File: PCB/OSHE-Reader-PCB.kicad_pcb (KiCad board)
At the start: 4 copper layers, 115 x 100 mm, 96 parts, among them J1 2171750001, J2 112L-TDA0, J3 Conn_01x24_MountingPin, J4 S2B-PH-K-SLFSN, Q1 Q_PNP_BCEC, Q2 Si1308EDL, SW1 SW_Push, SW2 SW_Push, SW3 SW_Push, SW4 SW_Push, SW5 SW_Push, U1 BQ2057CSNTR, U2 IRF7326D2TRPBF, U3 TPS5432DDAR

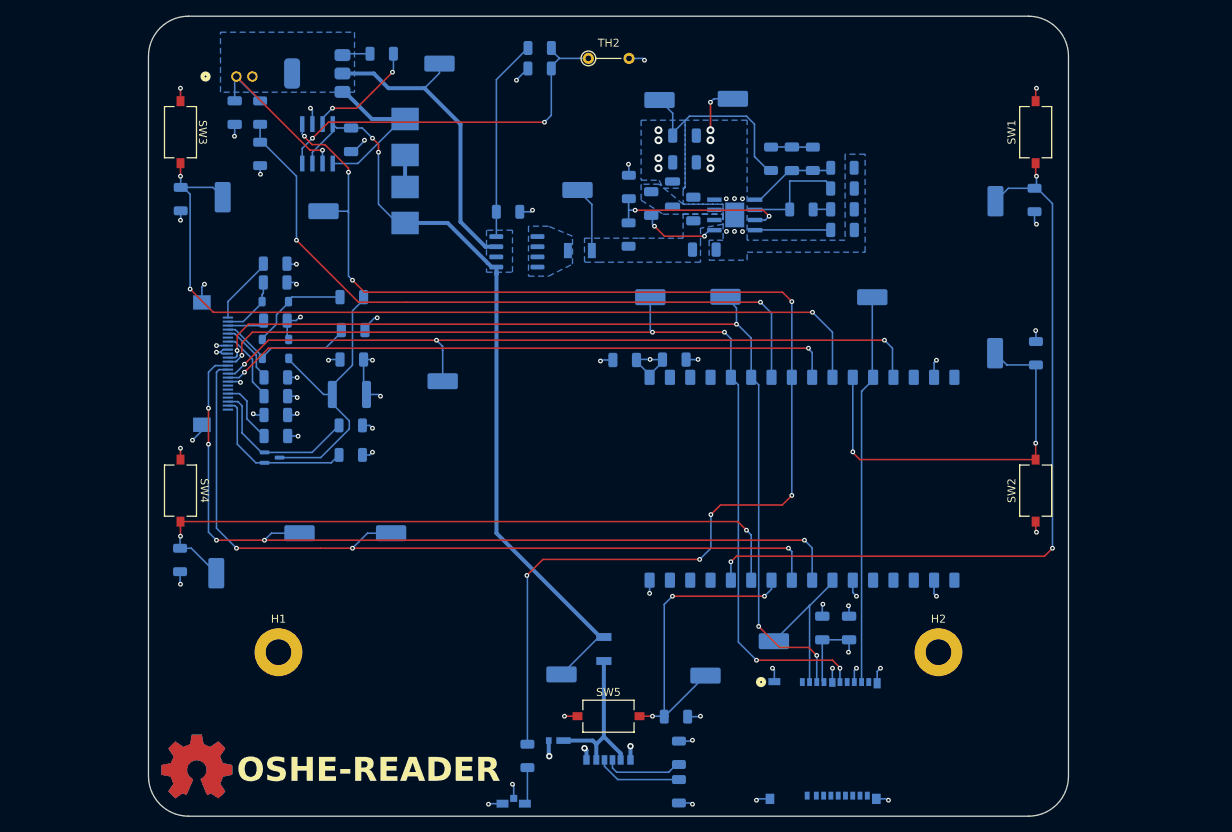
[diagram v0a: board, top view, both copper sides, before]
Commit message: Shuffled display connector around for fitting EPD ribbon cable position (also imported dxf for screen + bracket)
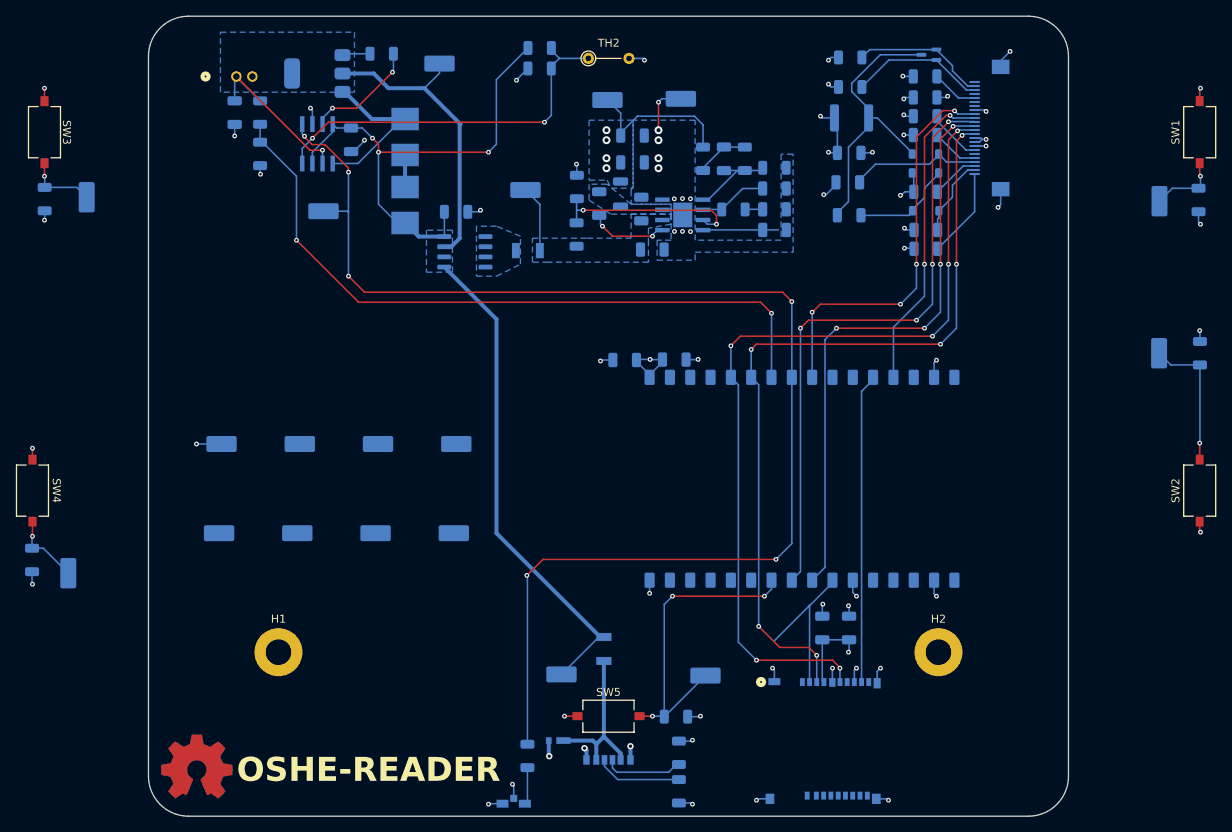
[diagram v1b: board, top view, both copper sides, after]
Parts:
- added TP_GND2: TestPoint, TestPoint:TestPoint_Keystone_5019_Miniature, B.Cu at (41.6, 134.0)
- R19: value 0.47R -> 0.47
- R20, TH2: value 10K -> 10k
- R21, R22: value 1M -> 100k
- R6: value 100K -> 100k
- moved J3 104.4 mm to (139.2, 94.5), turned to 90 degrees
- moved Q2 96.3 mm to (130.1, 85.3), turned to 180 degrees
- moved C17 92.8 mm to (129.6, 88.0), turned to 180 degrees
- moved C18 90.3 mm to (129.6, 90.7), turned to 180 degrees
- moved C19 88.4 mm to (129.6, 93.0), turned to 180 degrees
- moved C20 86.6 mm to (129.6, 95.4), turned to 180 degrees
- moved D2 85.2 mm to (129.6, 97.7), turned to 180 degrees
- moved D3 83.9 mm to (129.6, 100.1), turned to 0 degrees
- moved C21 82.9 mm to (129.6, 102.5), turned to 180 degrees
- moved D1 82.1 mm to (129.6, 104.8), turned to 0 degrees
- moved C22 81.6 mm to (129.7, 107.2), turned to 180 degrees
- moved C23 81.4 mm to (129.7, 109.6), turned to 180 degrees
- moved R20 79.8 mm to (120.2, 85.7), turned to 180 degrees
- moved R19 75.4 mm to (120.2, 89.3), turned to 180 degrees
- moved L2 71.7 mm to (120.4, 93.2), turned to 0 degrees
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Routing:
- net /Buttons/UpButton: track 110.3 -> 8.79 mm, vias 3 -> 1
- net /Buttons/LeftButton: track 98.1 -> 8.83 mm, vias 3 -> 1
- net /Buttons/DownButton: track 86.9 -> 9.17 mm, vias 2 -> 1
- net /EP_RESET: track 94.4 -> 39.2 mm, vias 3 -> 2
- net /EP_CS: track 107.8 -> 73.2 mm, vias 5 -> 4
- net /Buttons/RightButton: track 50.2 -> 17.6 mm, vias 2 -> 1
- net /EP_BUSY: track 77.9 -> 50.1 mm, vias 2 -> 4
- net /EP_D/C: track 103.4 -> 76.6 mm, vias 3 -> 4
- net /COPI: track 122.0 -> 99.9 mm, vias 4 -> 6
- net /SCK: track 124.5 -> 108.1 mm, vias 5 -> 6
- net /CIPO: track 48.7 -> 38.8 mm
- net Net-(U3-COMP): track 13.6 -> 8.55 mm
- net +3V3: track 62.8 -> 58.9 mm
- net /Display Connector/GDR: track 19.9 -> 16.8 mm
- net GND: track 91.7 -> 94.7 mm, vias 60 -> 61
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
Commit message: Did a bunch of work: - Updated footprint libs with proper 3d models to fix models dissapearing on update from pcb - Updated footprint libs with better silkscreen for drc - Re-did ESP32-C6 Footprint to support through hole AND castellated edges (espressif & waveshare) - Rerouted PCB around new MCU footprint - Minor cleanup on schematic + extra GND test point for convienience using O-Scope
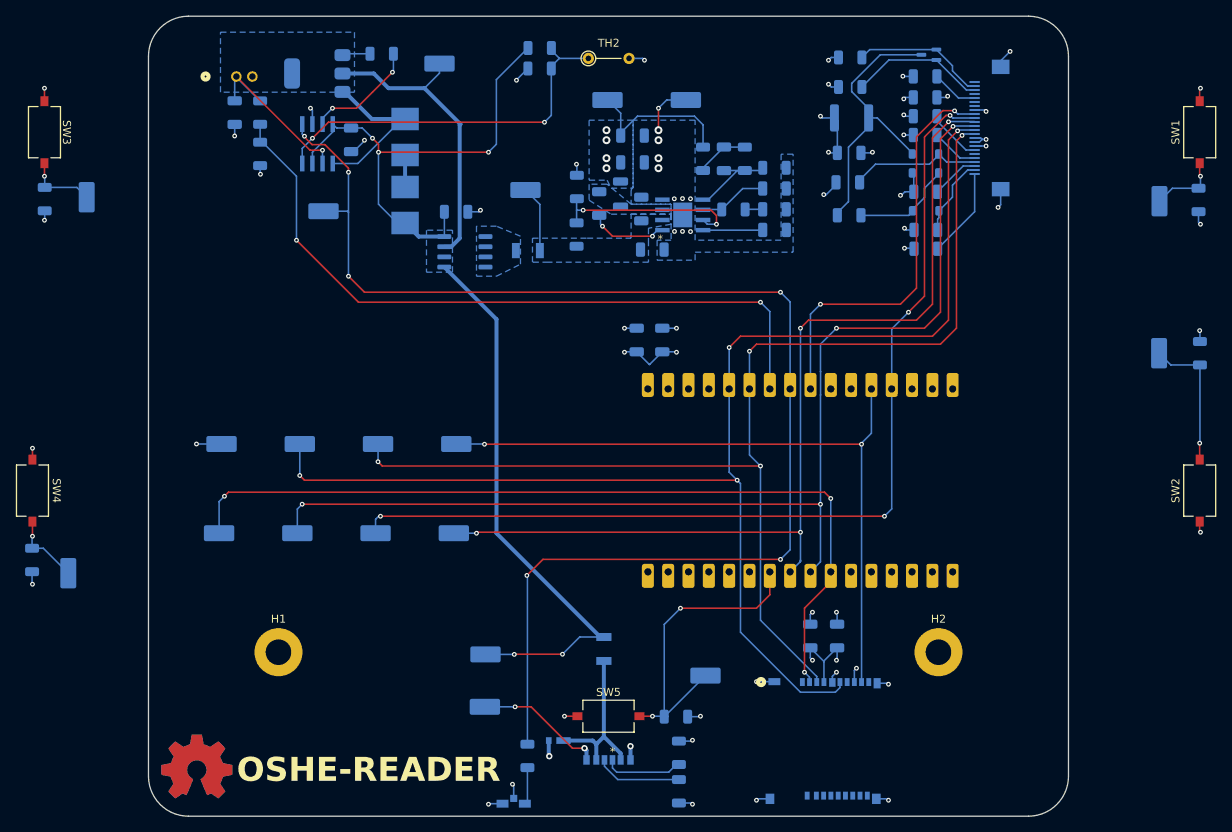
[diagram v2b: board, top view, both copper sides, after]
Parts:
- added TP_GND2: TestPoint, TestPoint:TestPoint_Keystone_5019_Miniature, B.Cu at (99.7, 91.0)
- moved TP_GND1 79.9 mm to (74.5, 166.8)
- moved TP_VBUS1 9.82 mm to (74.6, 160.3)
- moved C12 2.92 mm to (93.5, 121.0), turned to 90 degrees
- moved C13 2.87 mm to (96.7, 121.0), turned to 90 degrees
- moved C24 1.80 mm to (118.6, 158.0)
- moved C25 1.80 mm to (115.2, 158.0)
- moved U4 0.30 mm to (117.5, 138.5)
- renumbered TP_GND2 to TP_GND3
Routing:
- net /SD_CS: track 20.3 -> 108.6 mm, vias 0 -> 3
- net /EP_RESET: track 39.2 -> 122.5 mm, vias 2 -> 4
- net /EP_CS: track 73.2 -> 140.9 mm
- net /SCK: track 108.1 -> 166.6 mm, vias 6 -> 4
- net /CIPO: track 38.8 -> 88.3 mm, vias 0 -> 2
- net /COPI: track 99.9 -> 148.2 mm, vias 6 -> 4
- net /EP_D/C: track 76.6 -> 119.2 mm
- net /Battery Charging/VBUS: track 124.6 -> 133.1 mm, vias 3 -> 5
- net GND: track 94.7 -> 101.3 mm, vias 61 -> 58
- net Net-(U3-SS): track 9.46 -> 7.50 mm
- net /EP_BUSY: track 50.1 -> 51.7 mm, vias 4 -> 2
- net Net-(U4-GPIO0): track 87.7 -> 89.1 mm
- net +3V3: track 58.9 -> 58.1 mm, vias 15 -> 17
- net /Buttons/HomeButton: track 40.2 -> 40.0 mm, vias 3 -> 2

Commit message: Last updates for PCB order. Added revision number, fanicied logo, finished button positions, TODO: Blizzard T. Husky signature :P
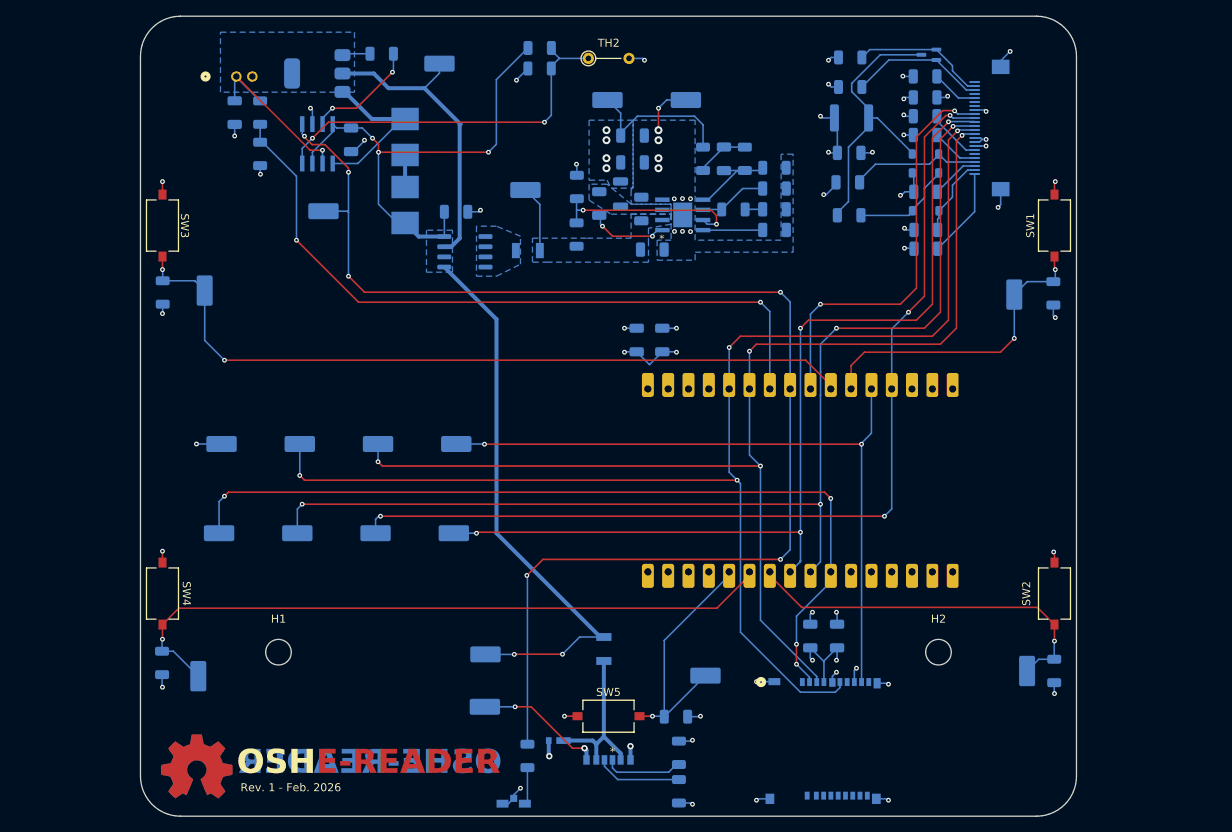
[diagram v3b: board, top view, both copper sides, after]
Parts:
- moved R17 43.7 mm to (145.7, 162.3), turned to -90 degrees
- moved TP_RIGHT1 43.0 mm to (142.3, 162.3)
- moved SW2 22.3 mm to (145.8, 152.7), turned to -90 degrees
- moved R16 21.6 mm to (145.6, 115.1)
- moved SW1 21.6 mm to (145.8, 106.7)
- moved TP_LEFT1 21.6 mm to (140.7, 115.3)
- moved R15 20.7 mm to (34.2, 161.3)
- moved SW4 20.7 mm to (34.2, 152.7)
- moved TP_DOWN1 20.7 mm to (38.7, 163.0)
- moved SW3 18.8 mm to (34.2, 106.7)
- moved TP_UP1 18.8 mm to (39.5, 114.8)
- moved R14 18.8 mm to (34.3, 115.0)
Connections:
- U4 pad 11: /Buttons/RightButton -> /Buttons/LeftButton
- U4 pad 21: /Buttons/LeftButton -> /Buttons/HomeButton
- U4 pad 23: /Buttons/HomeButton -> /Buttons/RightButton
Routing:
- net /Buttons/UpButton: track 8.79 -> 96.1 mm, vias 1 -> 2
- net /Buttons/DownButton: track 9.17 -> 85.5 mm
- net /Buttons/LeftButton: track 8.83 -> 39.0 mm, vias 1 -> 2
- net /Buttons/RightButton: track 17.6 -> 46.9 mm
- net /Buttons/HomeButton: track 40.0 -> 32.4 mm, vias 2 -> 1
- net /SD_CS: track 108.6 -> 109.4 mm, vias 3 -> 4
- net GND: track 101.3 -> 100.9 mm, vias 58 -> 57
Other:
- board size 115 x 100 mm -> 117 x 100 mm
- board text added: "E-READER"
- board text added: "OSH"
- board text added: "Rev. 1 - Feb. 2026"

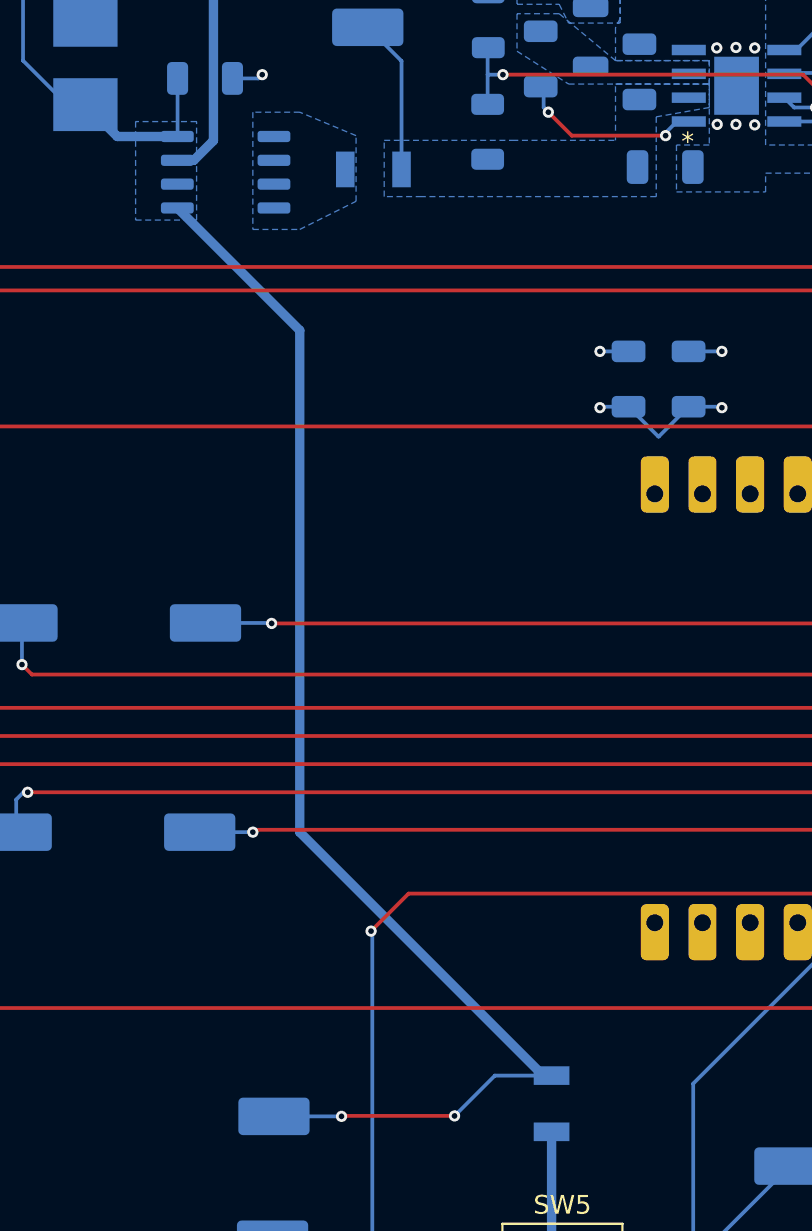
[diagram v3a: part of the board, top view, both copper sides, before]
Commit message: PCB and Schematic update
added the Schottky diode to PCB and Schematic
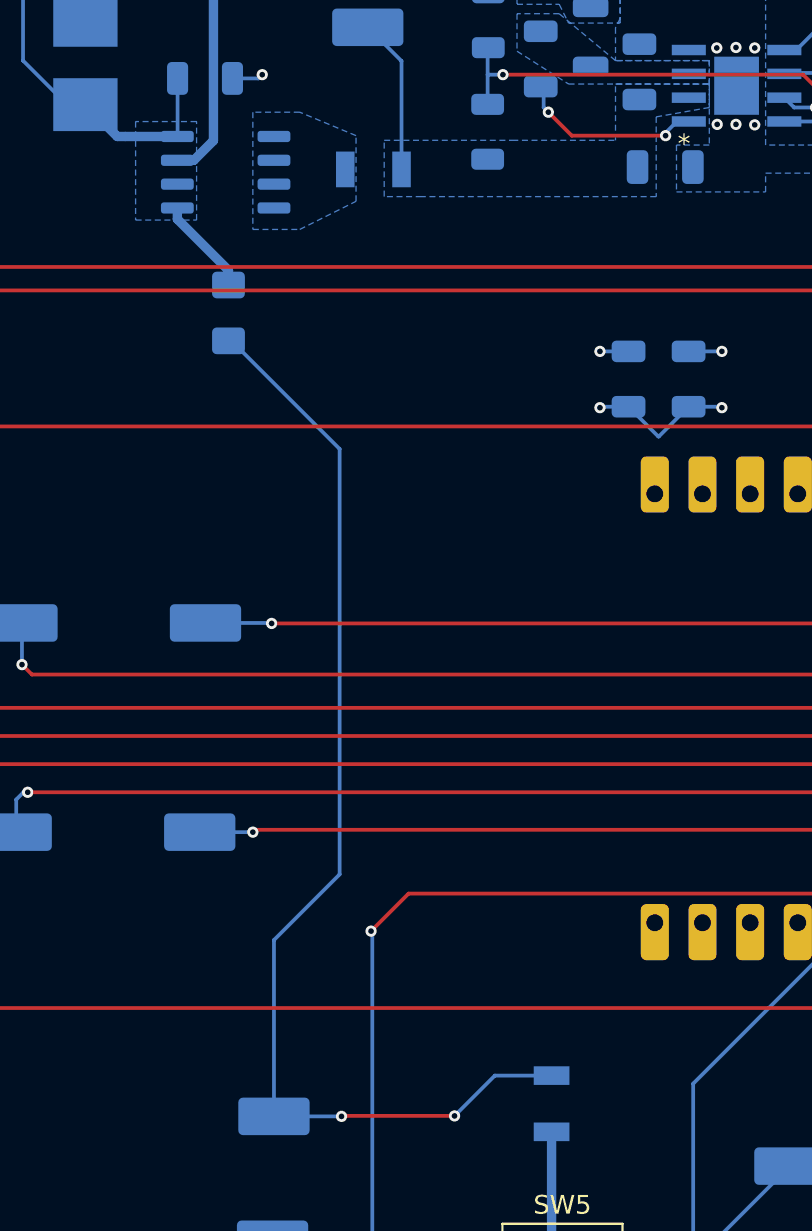
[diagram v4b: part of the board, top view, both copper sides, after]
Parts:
- added D4: D_Schottky, Diode_SMD:D_1206_3216Metric_Pad1.42x1.75mm_HandSolder, B.Cu at (72.2, 117.5)
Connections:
- F1 pad 2: /Battery Charging/VBUS -> Net-(D4-A)
- TP_VBUS1 pad 1: /Battery Charging/VBUS -> Net-(D4-A)
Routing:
- net /Battery Charging/VBUS: track 133.1 -> 67.9 mm, vias 5 -> 3
- net Net-(D4-A): track 0.00 -> 61.5 mm, vias 0 -> 2
